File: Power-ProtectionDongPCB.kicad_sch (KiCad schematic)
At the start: 2 parts, among them J1 Conn_01x02_Pin, J2 Conn_01x02_Socket

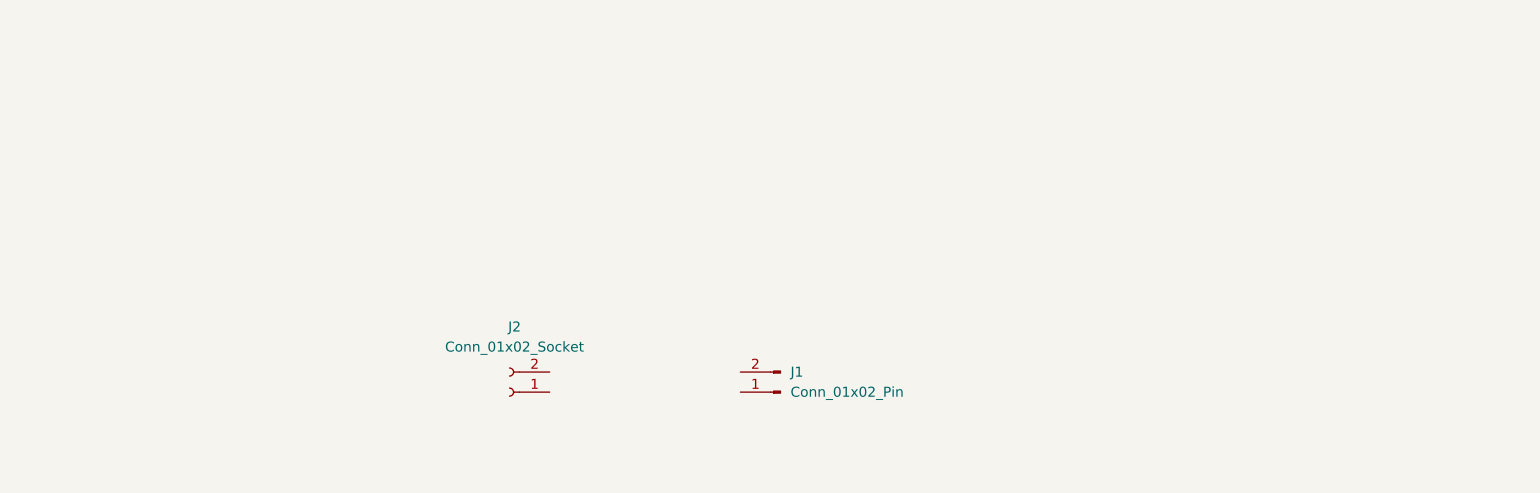
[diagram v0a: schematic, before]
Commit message: Fixed schematic
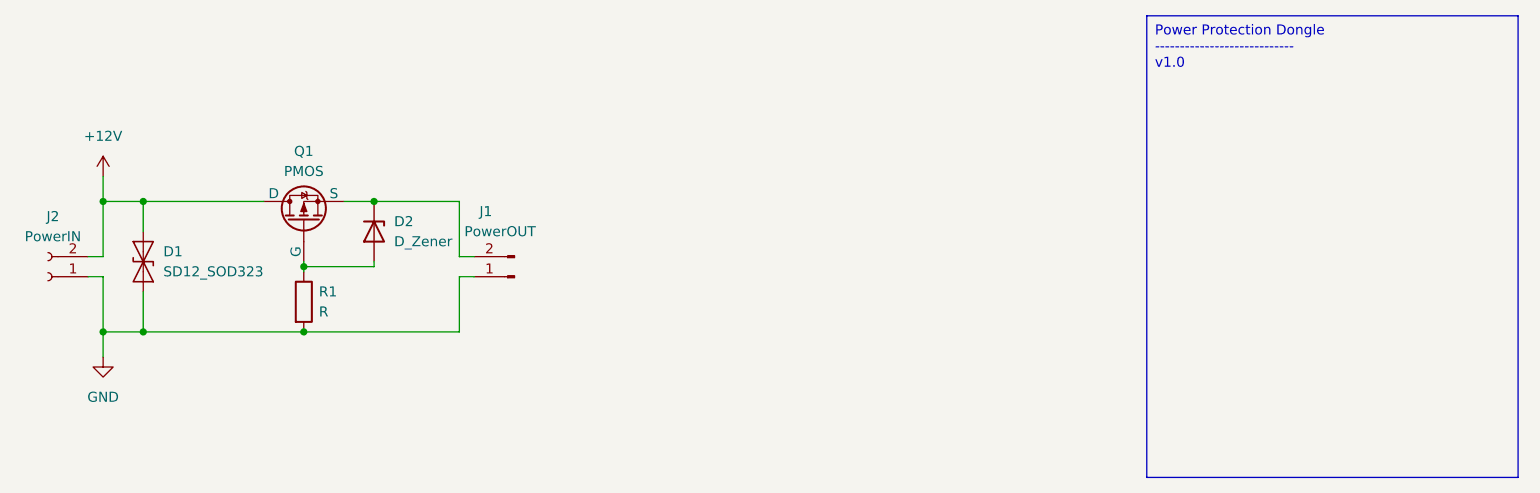
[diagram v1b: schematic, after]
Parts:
- added D1: SD12_SOD323, Diode_SMD:D_SOD-323, symbol Diode:SD12_SOD323
- added D2: D_Zener, symbol Device:D_Zener
- added Q1: PMOS, symbol Simulation_SPICE:PMOS
- added R1: R, symbol Device:R
- J1: value Conn_01x02_Pin -> PowerOUT; footprint (none) -> UTSVT_Connectors:Molex_MicroFit3.0_1x2xP3.00mm_PolarizingPeg_Vertical
- J2: value Conn_01x02_Socket -> PowerIN; footprint (none) -> UTSVT_Connectors:Molex_MicroFit3.0_1x2xP3.00mm_PolarizingPeg_Vertical
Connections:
- net GND: now reaches J1.1 (Pin_1)
- net GND: now also J2.1 (Pin_1), D1.2 (A2), R1.2
- net at J1.2 (Pin_2): now also D2.1 (K), Q1.3 (S)
- net +12V: now reaches J2.2 (Pin_2)
- net +12V: now also D1.1 (A1), Q1.1 (D)
- new net: D2.2 (A), Q1.2 (G), R1.1
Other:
- moved on the sheet: J1, J2
